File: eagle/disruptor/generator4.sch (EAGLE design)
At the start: 35 parts, among them IC1 NE555, IC2 74ALS04N, IC3 IR2110, IC4 7805TV, J1 PIN2F061.100, J2 PIN2F061.100, J3 PIN2F061.100, J4 PIN2F061.100, J5 PIN2F061.100, J6 PIN2F061.100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

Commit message: gen4b
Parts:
- added C14, C15: 1u, rcl:CPOL-EUE5-8.5
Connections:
- new net N$8: C14.-, C15.+, J2.1
- net GND: now also C15.-; no longer J2.1
- net N$6: now also C14.+
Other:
- moved on the sheet: J2
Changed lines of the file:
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@@
 <part name="B2" library="rectifier" deviceset="RECTIFIER-" device="GBU4"/>
 <part name="C13" library="resistor" deviceset="CPOL-US" device="E7.5-18"/>
+<part name="C14" library="rcl" deviceset="CPOL-EU" device="E5-8.5" value="1u"/>
+<part name="C15" library="rcl" deviceset="CPOL-EU" device="E5-8.5" value="1u"/>
 </parts>
 <sheets>
@@
 <instance part="R5" gate="G$1" x="220.98" y="63.5" rot="R180"/>
 <instance part="J1" gate="-1" x="238.76" y="76.2"/>
-<instance part="J2" gate="-1" x="238.76" y="50.8"/>
+<instance part="J2" gate="-1" x="248.92" y="76.2" rot="R180"/>
 <instance part="J3" gate="-1" x="10.16" y="160.02" rot="R180"/>
 <instance part="J4" gate="-1" x="12.7" y="149.86" rot="R180"/>
@@
 <instance part="B2" gate="G$1" x="25.4" y="78.74"/>
 <instance part="C13" gate="G$1" x="53.34" y="152.4"/>
+<instance part="C14" gate="G$1" x="254" y="93.98" smashed="yes">
+<attribute name="NAME" x="254.8848" y="94.5056" size="1.27" layer="95"/>
+<attribute name="VALUE" x="254.4977" y="89.598" size="1.27" layer="96"/>
+</instance>
+<instance part="C15" gate="G$1" x="254" y="63.5" smashed="yes">
+<attribute name="NAME" x="254.8848" y="64.0256" size="1.27" layer="95"/>
+<attribute name="VALUE" x="254.4977" y="59.118" size="1.27" layer="96"/>
+</instance>
 </instances>
 <busses>
@@
 <pinref part="GND1" gate="1" pin="GND"/>
 <wire x1="210.82" y1="66.04" x2="210.82" y2="50.8" width="0.1524" layer="91"/>
-<pinref part="Q2" gate="G$1" pin="S"/>
 <pinref part="R7" gate="G$1" pin="2"/>
 <wire x1="45.72" y1="50.8" x2="63.5" y2="50.8" width="0.1524" layer="91"/>
 <wire x1="63.5" y1="50.8" x2="210.82" y2="50.8" width="0.1524" layer="91"/>
-<wire x1="233.68" y1="50.8" x2="233.68" y2="60.96" width="0.1524" layer="91"/>
-<wire x1="226.06" y1="50.8" x2="233.68" y2="50.8" width="0.1524" layer="91"/>
 <wire x1="210.82" y1="50.8" x2="226.06" y2="50.8" width="0.1524" layer="91"/>
 <pinref part="GND6" gate="1" pin="GND"/>
@@
 <wire x1="20.32" y1="45.72" x2="45.72" y2="45.72" width="0.1524" layer="91"/>
 <wire x1="45.72" y1="45.72" x2="45.72" y2="50.8" width="0.1524" layer="91"/>
-<pinref part="J2" gate="-1" pin="1"/>
+<pinref part="C15" gate="G$1" pin="-"/>
+<wire x1="226.06" y1="50.8" x2="233.68" y2="50.8" width="0.1524" layer="91"/>
+<wire x1="233.68" y1="50.8" x2="254" y2="50.8" width="0.1524" layer="91"/>
+<wire x1="254" y1="50.8" x2="254" y2="58.42" width="0.1524" layer="91"/>
+<pinref part="Q2" gate="G$1" pin="S"/>
+<wire x1="233.68" y1="60.96" x2="233.68" y2="50.8" width="0.1524" layer="91"/>
 </segment>
 <segment>
@@
 <wire x1="35.56" y1="78.74" x2="35.56" y2="109.22" width="0.1524" layer="91"/>
 <wire x1="35.56" y1="109.22" x2="45.72" y2="109.22" width="0.1524" layer="91"/>
-</segment>
-</net>
+<pinref part="C14" gate="G$1" pin="+"/>
+<wire x1="254" y1="96.52" x2="254" y2="109.22" width="0.1524" layer="91"/>
+<wire x1="254" y1="109.22" x2="233.68" y2="109.22" width="0.1524" layer="91"/>
+</segment>
+</net>
+<net name="N$8" class="0">
+<segment>
+<pinref part="J2" gate="-1" pin="1"/>
+<pinref part="C15" gate="G$1" pin="+"/>
+<wire x1="254" y1="76.2" x2="254" y2="66.04" width="0.1524" layer="91"/>
+<pinref part="C14" gate="G$1" pin="-"/>
+<wire x1="254" y1="76.2" x2="254" y2="88.9" width="0.1524" layer="91"/>
+</segment>
+</net>

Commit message: generator 4 is the correct way.
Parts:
- C14, C15: value 1u -> 50u
- C7: value 1u -> min 12 nF
- R4, R5: value 100 -> 10
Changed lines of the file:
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@@
 <part name="D1" library="diode" deviceset="DIODE-" device="D-7.5" value="UF4004"/>
 <part name="C8" library="rcl" deviceset="CPOL-EU" device="E5-8.5" value="1u"/>
-<part name="C7" library="rcl" deviceset="CPOL-EU" device="E5-8.5" value="1u"/>
+<part name="C7" library="rcl" deviceset="CPOL-EU" device="E5-8.5" value="min 12 nF"/>
 <part name="FRAME1" library="frames" deviceset="A4L-LOC" device=""/>
 <part name="IC1" library="st-microelectronics" deviceset="NE555" device=""/>
@@
 <part name="C5" library="rcl" deviceset="CPOL-EU" device="E5-8.5" value="1u"/>
 <part name="GND8" library="supply1" deviceset="GND" device=""/>
-<part name="R4" library="rcl" deviceset="R-US_" device="0207/10" value="100"/>
-<part name="R5" library="rcl" deviceset="R-US_" device="0207/10" value="100"/>
+<part name="R4" library="rcl" deviceset="R-US_" device="0207/10" value="10"/>
+<part name="R5" library="rcl" deviceset="R-US_" device="0207/10" value="10"/>
 <part name="J1" library="con-faston" deviceset="PIN2" device="F061.100"/>
 <part name="J2" library="con-faston" deviceset="PIN2" device="F061.100"/>
@@
 <part name="B2" library="rectifier" deviceset="RECTIFIER-" device="GBU4"/>
 <part name="C13" library="resistor" deviceset="CPOL-US" device="E7.5-18"/>
-<part name="C14" library="rcl" deviceset="CPOL-EU" device="E5-8.5" value="1u"/>
-<part name="C15" library="rcl" deviceset="CPOL-EU" device="E5-8.5" value="1u"/>
+<part name="C14" library="rcl" deviceset="CPOL-EU" device="E5-8.5" value="50u"/>
+<part name="C15" library="rcl" deviceset="CPOL-EU" device="E5-8.5" value="50u"/>
 </parts>
 <sheets>

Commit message: gen 4 board layout done.
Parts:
- removed B2: RECTIFIER-GBU4, rectifier:RECTIFIER-GBU4
- C14, C15: value 50u -> 470u; device rcl:CPOL-EUE5-8.5 -> rcl:CPOL-EUE7.5-16
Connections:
- removed net N$4: B2.AC1, J5.1
- removed net N$5: B2.AC2, J6.1
- net GND: now also J6.1; no longer B2.-
- net N$6: now also J5.1; no longer B2.+

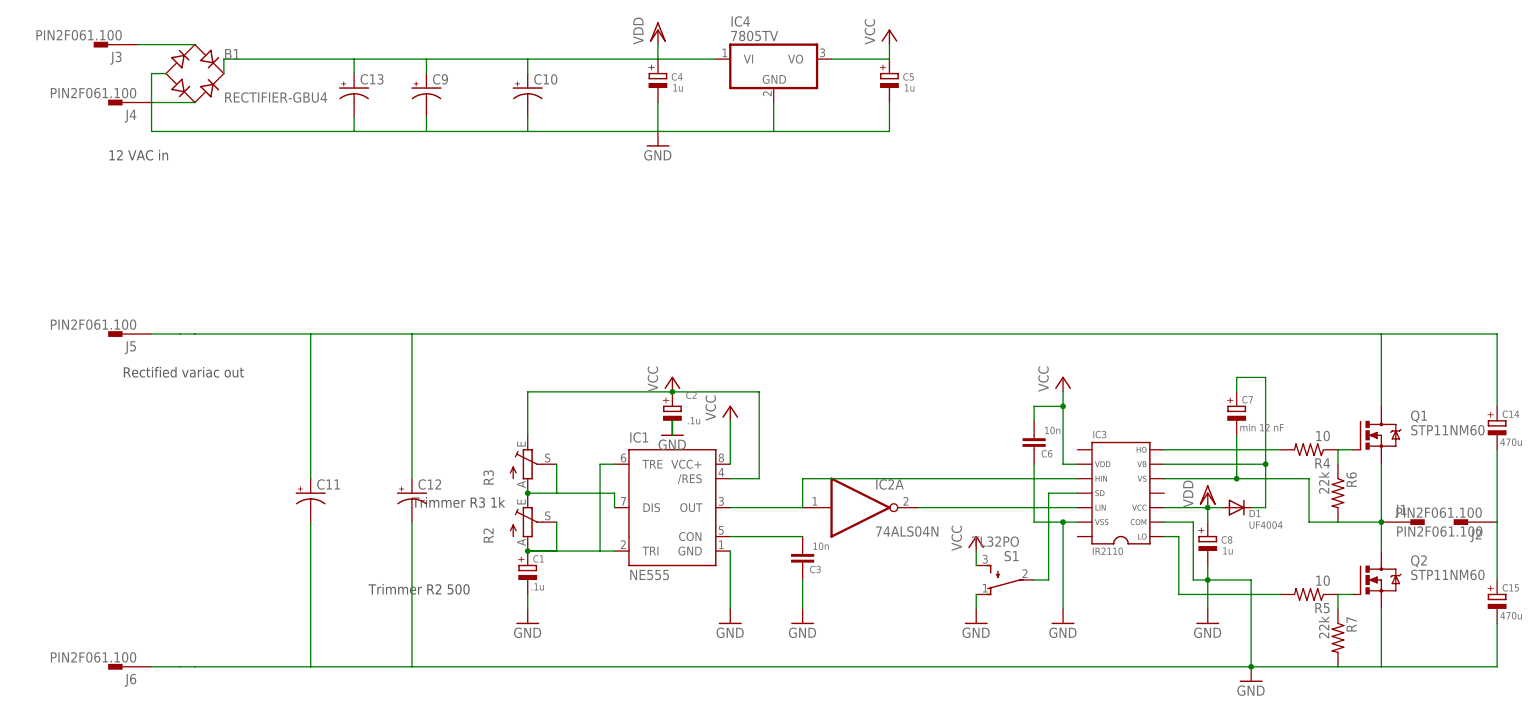
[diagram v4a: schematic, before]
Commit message: beefier cap values
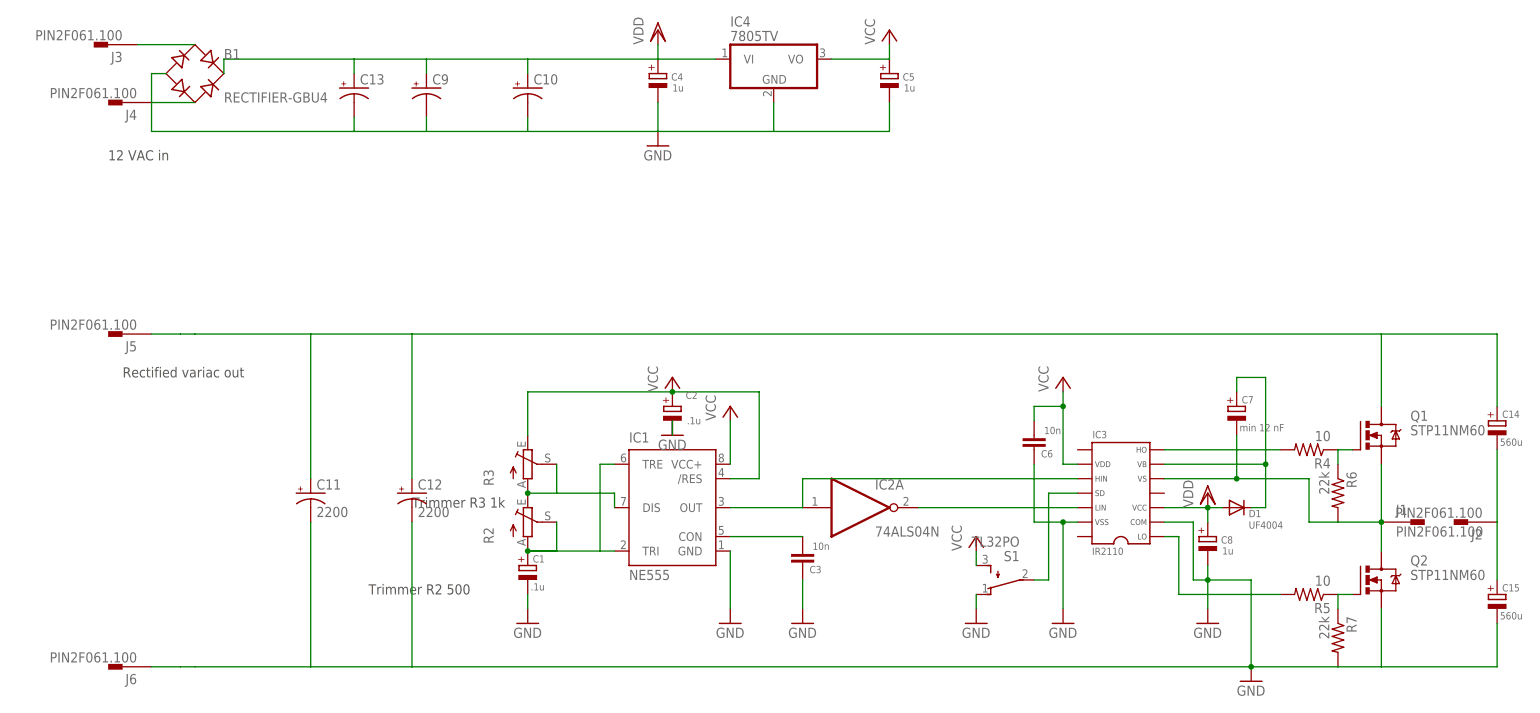
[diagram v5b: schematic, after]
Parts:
- C11, C12: value (none) -> 2200
- C14, C15: value 470u -> 560u
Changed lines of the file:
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@@
 <grid distance="0.1" unitdist="inch" unit="inch" style="lines" multiple="1" display="no" altdistance="0.01" altunitdist="inch" altunit="inch"/>
 <layers>
-<layer number="1" name="Top" color="4" fill="1" visible="no" active="no"/>
-<layer number="2" name="Route2" color="1" fill="3" visible="no" active="no"/>
-<layer number="3" name="Route3" color="4" fill="3" visible="no" active="no"/>
-<layer number="4" name="Route4" color="1" fill="4" visible="no" active="no"/>
-<layer number="5" name="Route5" color="4" fill="4" visible="no" active="no"/>
-<layer number="6" name="Route6" color="1" fill="8" visible="no" active="no"/>
-<layer number="7" name="Route7" color="4" fill="8" visible="no" active="no"/>
-<layer number="8" name="Route8" color="1" fill="2" visible="no" active="no"/>
-<layer number="9" name="Route9" color="4" fill="2" visible="no" active="no"/>
-<layer number="10" name="Route10" color="1" fill="7" visible="no" active="no"/>
-<layer number="11" name="Route11" color="4" fill="7" visible="no" active="no"/>
-<layer number="12" name="Route12" color="1" fill="5" visible="no" active="no"/>
-<layer number="13" name="Route13" color="4" fill="5" visible="no" active="no"/>
-<layer number="14" name="Route14" color="1" fill="6" visible="no" active="no"/>
-<layer number="15" name="Route15" color="4" fill="6" visible="no" active="no"/>
-<layer number="16" name="Bottom" color="1" fill="1" visible="no" active="no"/>
-<layer number="17" name="Pads" color="2" fill="1" visible="no" active="no"/>
-<layer number="18" name="Vias" color="2" fill="1" visible="no" active="no"/>
-<layer number="19" name="Unrouted" color="6" fill="1" visible="no" active="no"/>
-<layer number="20" name="Dimension" color="15" fill="1" visible="no" active="no"/>
-<layer number="21" name="tPlace" color="7" fill="1" visible="no" active="no"/>
-<layer number="22" name="bPlace" color="7" fill="1" visible="no" active="no"/>
-<layer number="23" name="tOrigins" color="15" fill="1" visible="no" active="no"/>
-<layer number="24" name="bOrigins" color="15" fill="1" visible="no" active="no"/>
-<layer number="25" name="tNames" color="7" fill="1" visible="no" active="no"/>
-<layer number="26" name="bNames" color="7" fill="1" visible="no" active="no"/>
-<layer number="27" name="tValues" color="7" fill="1" visible="no" active="no"/>
-<layer number="28" name="bValues" color="7" fill="1" visible="no" active="no"/>
+<layer number="1" name="Top" color="4" fill="1" visible="yes" active="no"/>
+<layer number="2" name="Route2" color="1" fill="3" visible="yes" active="no"/>
+<layer number="3" name="Route3" color="4" fill="3" visible="yes" active="no"/>
+<layer number="4" name="Route4" color="1" fill="4" visible="yes" active="no"/>
+<layer number="5" name="Route5" color="4" fill="4" visible="yes" active="no"/>
+<layer number="6" name="Route6" color="1" fill="8" visible="yes" active="no"/>
+<layer number="7" name="Route7" color="4" fill="8" visible="yes" active="no"/>
+<layer number="8" name="Route8" color="1" fill="2" visible="yes" active="no"/>
+<layer number="9" name="Route9" color="4" fill="2" visible="yes" active="no"/>
+<layer number="10" name="Route10" color="1" fill="7" visible="yes" active="no"/>
+<layer number="11" name="Route11" color="4" fill="7" visible="yes" active="no"/>
+<layer number="12" name="Route12" color="1" fill="5" visible="yes" active="no"/>
+<layer number="13" name="Route13" color="4" fill="5" visible="yes" active="no"/>
+<layer number="14" name="Route14" color="1" fill="6" visible="yes" active="no"/>
+<layer number="15" name="Route15" color="4" fill="6" visible="yes" active="no"/>
+<layer number="16" name="Bottom" color="1" fill="1" visible="yes" active="no"/>
+<layer number="17" name="Pads" color="2" fill="1" visible="yes" active="no"/>
+<layer number="18" name="Vias" color="2" fill="1" visible="yes" active="no"/>
+<layer number="19" name="Unrouted" color="6" fill="1" visible="yes" active="no"/>
+<layer number="20" name="Dimension" color="15" fill="1" visible="yes" active="no"/>
+<layer number="21" name="tPlace" color="7" fill="1" visible="yes" active="no"/>
+<layer number="22" name="bPlace" color="7" fill="1" visible="yes" active="no"/>
+<layer number="23" name="tOrigins" color="15" fill="1" visible="yes" active="no"/>
+<layer number="24" name="bOrigins" color="15" fill="1" visible="yes" active="no"/>
+<layer number="25" name="tNames" color="7" fill="1" visible="yes" active="no"/>
+<layer number="26" name="bNames" color="7" fill="1" visible="yes" active="no"/>
+<layer number="27" name="tValues" color="7" fill="1" visible="yes" active="no"/>
+<layer number="28" name="bValues" color="7" fill="1" visible="yes" active="no"/>
 <layer number="29" name="tStop" color="7" fill="3" visible="no" active="no"/>
 <layer number="30" name="bStop" color="7" fill="6" visible="no" active="no"/>
@@
 <layer number="35" name="tGlue" color="7" fill="4" visible="no" active="no"/>
 <layer number="36" name="bGlue" color="7" fill="5" visible="no" active="no"/>
-<layer number="37" name="tTest" color="7" fill="1" visible="no" active="no"/>
-<layer number="38" name="bTest" color="7" fill="1" visible="no" active="no"/>
+<layer number="37" name="tTest" color="7" fill="1" visible="yes" active="no"/>
+<layer number="38" name="bTest" color="7" fill="1" visible="yes" active="no"/>
 <layer number="39" name="tKeepout" color="4" fill="11" visible="no" active="no"/>
 <layer number="40" name="bKeepout" color="1" fill="11" visible="no" active="no"/>
@@
 <layer number="44" name="Drills" color="7" fill="1" visible="no" active="no"/>
 <layer number="45" name="Holes" color="7" fill="1" visible="no" active="no"/>
-<layer number="46" name="Milling" color="3" fill="1" visible="no" active="no"/>
-<layer number="47" name="Measures" color="7" fill="1" visible="no" active="no"/>
-<layer number="48" name="Document" color="7" fill="1" visible="no" active="no"/>
-<layer number="49" name="Reference" color="7" fill="1" visible="no" active="no"/>
-<layer number="50" name="dxf" color="7" fill="1" visible="no" active="no"/>
-<layer number="51" name="tDocu" color="7" fill="1" visible="no" active="no"/>
-<layer number="52" name="bDocu" color="7" fill="1" visible="no" active="no"/>
-<layer number="53" name="tGND_GNDA" color="7" fill="9" visible="no" active="no"/>
-<layer number="54" name="bGND_GNDA" color="1" fill="9" visible="no" active="no"/>
+<layer number="46" name="Milling" color="3" fill="1" visible="yes" active="no"/>
+<layer number="47" name="Measures" color="7" fill="1" visible="yes" active="no"/>
+<layer number="48" name="Document" color="7" fill="1" visible="yes" active="no"/>
+<layer number="49" name="Reference" color="7" fill="1" visible="yes" active="no"/>
+<layer number="50" name="dxf" color="7" fill="1" visible="yes" active="no"/>
+<layer number="51" name="tDocu" color="7" fill="1" visible="yes" active="no"/>
+<layer number="52" name="bDocu" color="7" fill="1" visible="yes" active="no"/>
+<layer number="53" name="tGND_GNDA" color="7" fill="9" visible="yes" active="no"/>
+<layer number="54" name="bGND_GNDA" color="1" fill="9" visible="yes" active="no"/>
 <layer number="91" name="Nets" color="2" fill="1" visible="yes" active="yes"/>
 <layer number="92" name="Busses" color="1" fill="1" visible="yes" active="yes"/>
@@
 <part name="C9" library="resistor" deviceset="CPOL-US" device="E7.5-18"/>
 <part name="C10" library="resistor" deviceset="CPOL-US" device="E7.5-18"/>
-<part name="C11" library="resistor" deviceset="CPOL-US" device="E10-35"/>
-<part name="C12" library="resistor" deviceset="CPOL-US" device="E10-35"/>
+<part name="C11" library="resistor" deviceset="CPOL-US" device="E10-35" value="2200"/>
+<part name="C12" library="resistor" deviceset="CPOL-US" device="E10-35" value="2200"/>
 <part name="C13" library="resistor" deviceset="CPOL-US" device="E7.5-18"/>
-<part name="C14" library="rcl" deviceset="CPOL-EU" device="E7.5-16" value="470u"/>
-<part name="C15" library="rcl" deviceset="CPOL-EU" device="E7.5-16" value="470u"/>
+<part name="C14" library="rcl" deviceset="CPOL-EU" device="E7.5-16" value="560u"/>
+<part name="C15" library="rcl" deviceset="CPOL-EU" device="E7.5-16" value="560u"/>
 </parts>
 <sheets>
